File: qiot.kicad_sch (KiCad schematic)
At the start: 0 parts

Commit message: add base
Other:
- removed sheet 12_IMX1062
- removed sheet 13_ethernet
- removed sheet 14_RAM
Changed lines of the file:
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@@
-	)
-	(sheet
-		(at 104.775 146.685)
-		(size 29.21 15.24)
-		(exclude_from_sim no)
-		(in_bom yes)
-		(on_board yes)
-		(dnp no)
-		(fields_autoplaced yes)
-		(stroke
-			(width 0.1524)
-			(type solid)
-		)
-		(fill
-			(color 0 0 0 0.0000)
-		)
-		(property "Sheetname" "13_ethernet"
-			(at 104.775 145.9734 0)
-			(effects
-				(font
-					(size 1.27 1.27)
-				)
-				(justify left bottom)
-			)
-		)
-		(property "Sheetfile" "Ethernet.kicad_sch"
-			(at 104.775 162.5096 0)
-			(effects
-				(font
-					(size 1.27 1.27)
-				)
-				(justify left top)
-			)
-		)
-		(instances
-			(project "qiot"
-				(path "/0db193be-516d-4409-bb62-b8733a9e8874"
-					(page "14")
-				)
-			)
-		)
-	)
-	(sheet
-		(at 54.61 140.335)
-		(size 27.94 7.62)
-		(exclude_from_sim no)
-		(in_bom yes)
-		(on_board yes)
-		(dnp no)
-		(fields_autoplaced yes)
-		(stroke
-			(width 0.1524)
-			(type solid)
-		)
-		(fill
-			(color 0 0 0 0.0000)
-		)
-		(property "Sheetname" "12_IMX1062"
-			(at 54.61 139.6234 0)
-			(effects
-				(font
-					(size 1.27 1.27)
-				)
-				(justify left bottom)
-			)
-		)
-		(property "Sheetfile" "12_imx1062.kicad_sch"
-			(at 54.61 148.5396 0)
-			(effects
-				(font
-					(size 1.27 1.27)
-				)
-				(justify left top)
-			)
-		)
-		(instances
-			(project "qiot"
-				(path "/0db193be-516d-4409-bb62-b8733a9e8874"
-					(page "13")
-				)
-			)
-		)
 	)
 	(sheet
@@
 				)
 			)
-		)
-	)
-	(sheet
-		(at 143.51 135.255)
-		(size 27.305 17.78)
-		(exclude_from_sim no)
-		(in_bom yes)
-		(on_board yes)
-		(dnp no)
-		(fields_autoplaced yes)
-		(stroke
-			(width 0.1524)
-			(type solid)
-		)
-		(fill
-			(color 0 0 0 0.0000)
-		)
-		(property "Sheetname" "14_RAM"
-			(at 143.51 134.5434 0)
-			(effects
-				(font
-					(size 1.27 1.27)
-				)
-				(justify left bottom)
-			)
-		)
-		(property "Sheetfile" "14_RAM.kicad_sch"
-			(at 143.51 153.6196 0)
-			(effects
-				(font
-					(size 1.27 1.27)
-				)
-				(justify left top)
-			)
-		)
-		(instances
-			(project "qiot"
-				(path "/0db193be-516d-4409-bb62-b8733a9e8874"
-					(page "15")
-				)
-			)

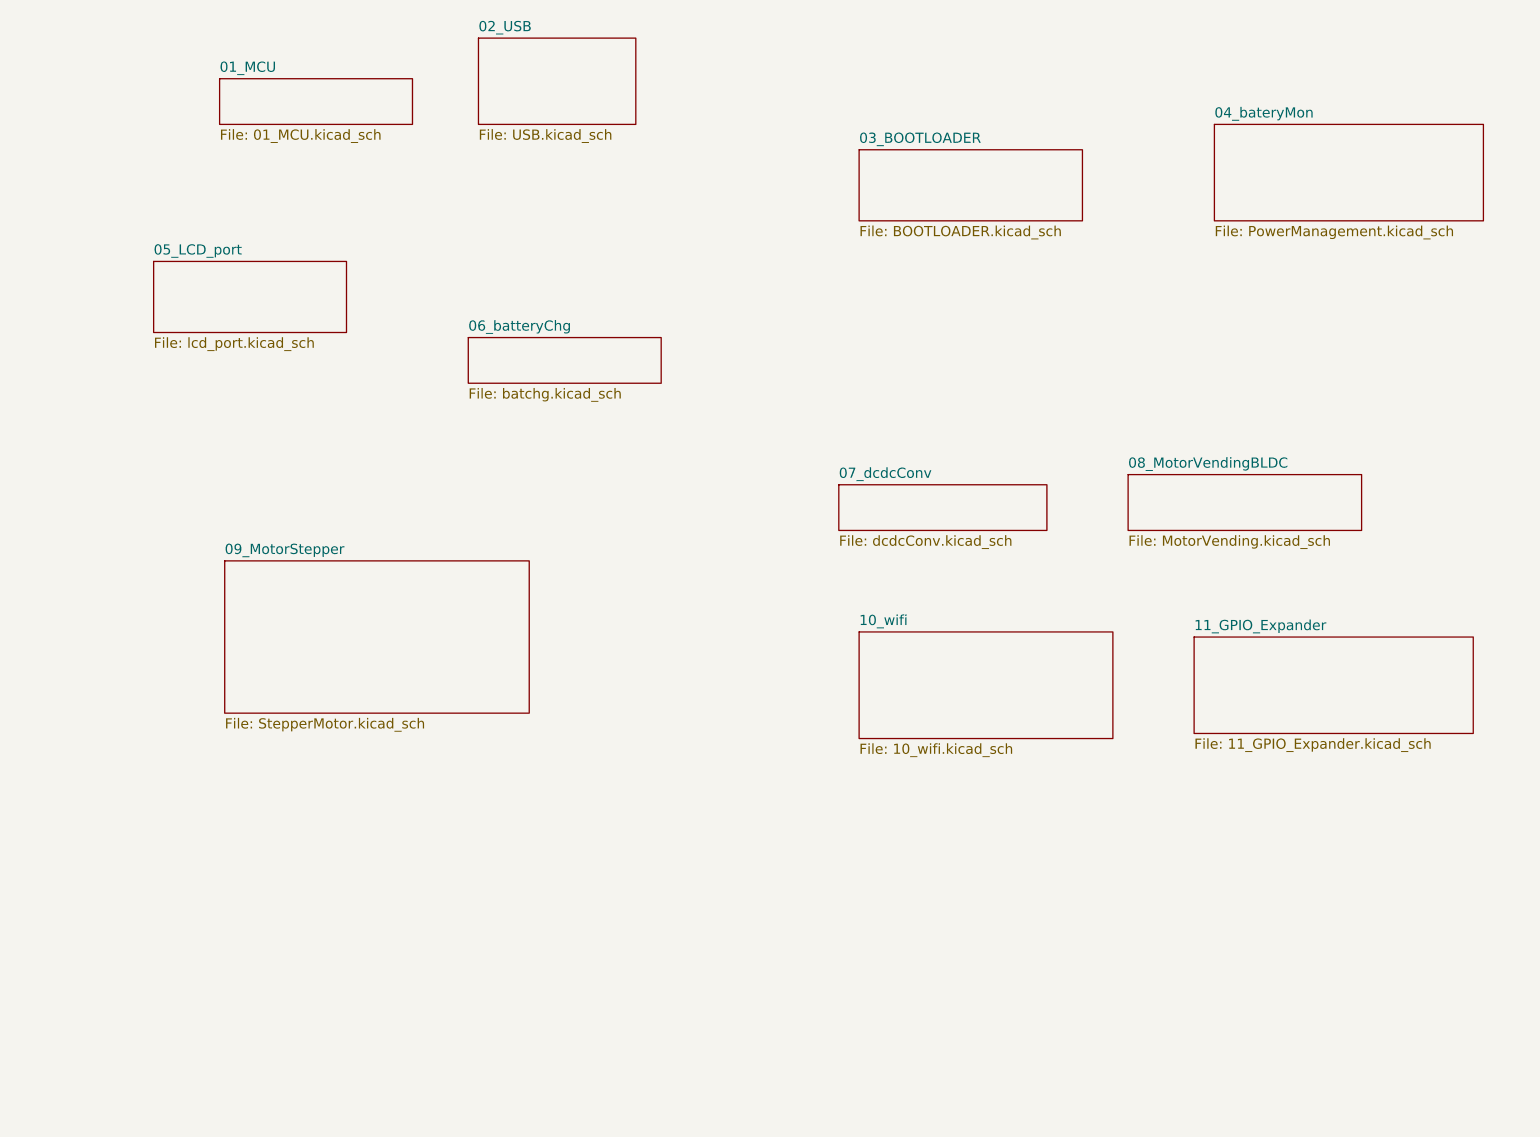
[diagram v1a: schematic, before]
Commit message: add revision to motor
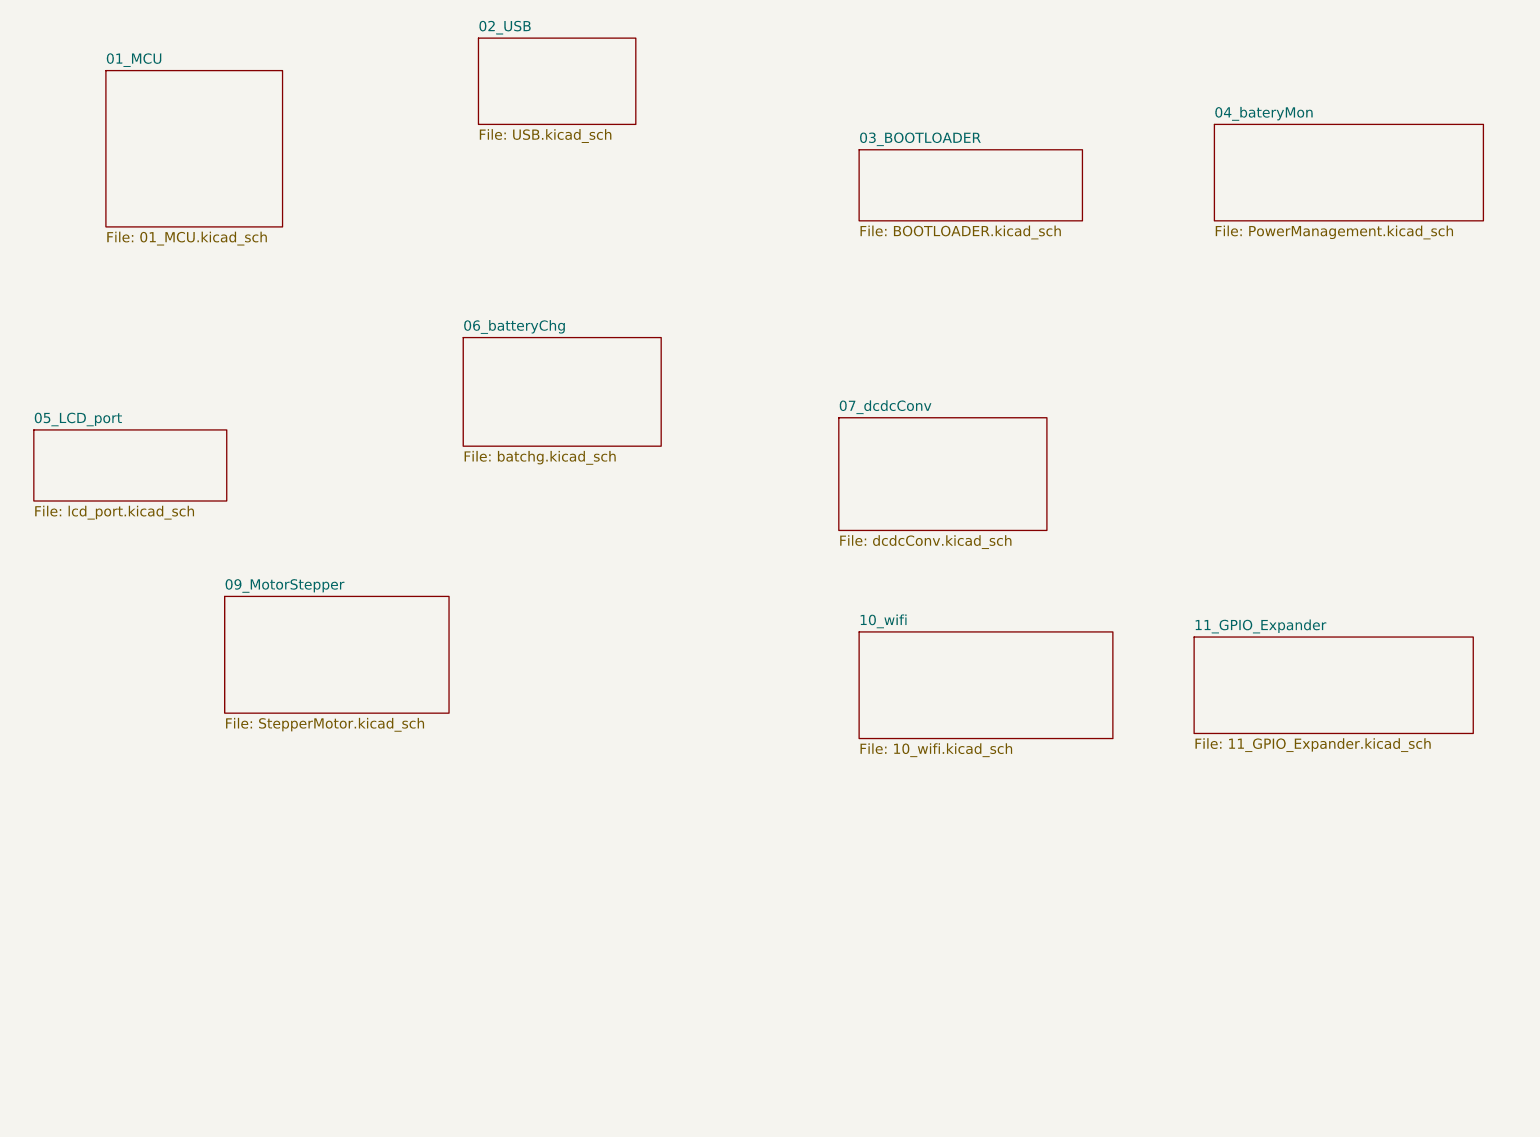
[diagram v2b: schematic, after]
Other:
- removed sheet 08_MotorVendingBLDC
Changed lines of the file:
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@@
 	)
 	(sheet
-		(at 80.645 104.775)
-		(size 38.1 19.05)
+		(at 80.645 109.22)
+		(size 28.067 14.605)
 		(exclude_from_sim no)
 		(in_bom yes)
@@
 		)
 		(property "Sheetname" "09_MotorStepper"
-			(at 80.645 104.0634 0)
+			(at 80.645 108.5084 0)
 			(effects
 				(font
@@
 	)
 	(sheet
-		(at 157.48 95.25)
-		(size 26.035 5.715)
+		(at 157.48 86.868)
+		(size 26.035 14.097)
 		(exclude_from_sim no)
 		(in_bom yes)
@@
 		)
 		(property "Sheetname" "07_dcdcConv"
-			(at 157.48 94.5384 0)
+			(at 157.48 86.1564 0)
 			(effects
 				(font
@@
 	)
 	(sheet
-		(at 193.675 93.98)
-		(size 29.21 6.985)
-		(exclude_from_sim no)
-		(in_bom yes)
-		(on_board yes)
-		(dnp no)
-		(fields_autoplaced yes)
-		(stroke
-			(width 0.1524)
-			(type solid)
-		)
-		(fill
-			(color 0 0 0 0.0000)
-		)
-		(property "Sheetname" "08_MotorVendingBLDC"
-			(at 193.675 93.2684 0)
-			(effects
-				(font
-					(size 1.27 1.27)
-				)
-				(justify left bottom)
-			)
-		)
-		(property "Sheetfile" "MotorVending.kicad_sch"
-			(at 193.675 101.5496 0)
-			(effects
-				(font
-					(size 1.27 1.27)
-				)
-				(justify left top)
-			)
-		)
-		(instances
-			(project "qiot"
-				(path "/0db193be-516d-4409-bb62-b8733a9e8874"
-					(page "9")
-				)
-			)
-		)
-	)
-	(sheet
-		(at 71.755 67.31)
+		(at 56.769 88.392)
 		(size 24.13 8.89)
 		(exclude_from_sim no)
@@
 		)
 		(property "Sheetname" "05_LCD_port"
-			(at 71.755 66.5984 0)
+			(at 56.769 87.6804 0)
 			(effects
 				(font
@@
 		)
 		(property "Sheetfile" "lcd_port.kicad_sch"
-			(at 71.755 76.7846 0)
+			(at 56.769 97.8666 0)
 			(effects
 				(font
@@
 	)
 	(sheet
-		(at 80.01 44.45)
-		(size 24.13 5.715)
+		(at 65.786 43.434)
+		(size 22.098 19.558)
 		(exclude_from_sim no)
 		(in_bom yes)
@@
 		)
 		(property "Sheetname" "01_MCU"
-			(at 80.01 43.7384 0)
+			(at 65.786 42.7224 0)
 			(effects
 				(font
@@
 		)
 		(property "Sheetfile" "01_MCU.kicad_sch"
-			(at 80.01 50.7496 0)
+			(at 65.786 63.5766 0)
 			(effects
 				(font
@@
 	)
 	(sheet
-		(at 111.125 76.835)
-		(size 24.13 5.715)
+		(at 110.49 76.835)
+		(size 24.765 13.589)
 		(exclude_from_sim no)
 		(in_bom yes)
@@
 		)
 		(property "Sheetname" "06_batteryChg"
-			(at 111.125 76.1234 0)
+			(at 110.49 76.1234 0)
 			(effects
 				(font
@@
 		)
 		(property "Sheetfile" "batchg.kicad_sch"
-			(at 111.125 83.1346 0)
-			(effects
-				(font
+			(at 110.49 91.0086 0)
+			(effects
+				(font

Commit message: gema
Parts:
- added FID1, FID2, FID3: Fiducial, Fiducial:Fiducial_1.5mm_Mask3mm, symbol Mechanical:Fiducial
- added H1, H2, H3, H4: MountingHole, MountingHole:MountingHole_2.7mm_M2.5, symbol Mechanical:MountingHole
